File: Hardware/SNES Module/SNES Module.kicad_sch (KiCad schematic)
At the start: 4 parts, among them J1 Conn_01x31_Pin, J2 Conn_01x31_Pin, J3 Conn_02x31_Top_Bottom

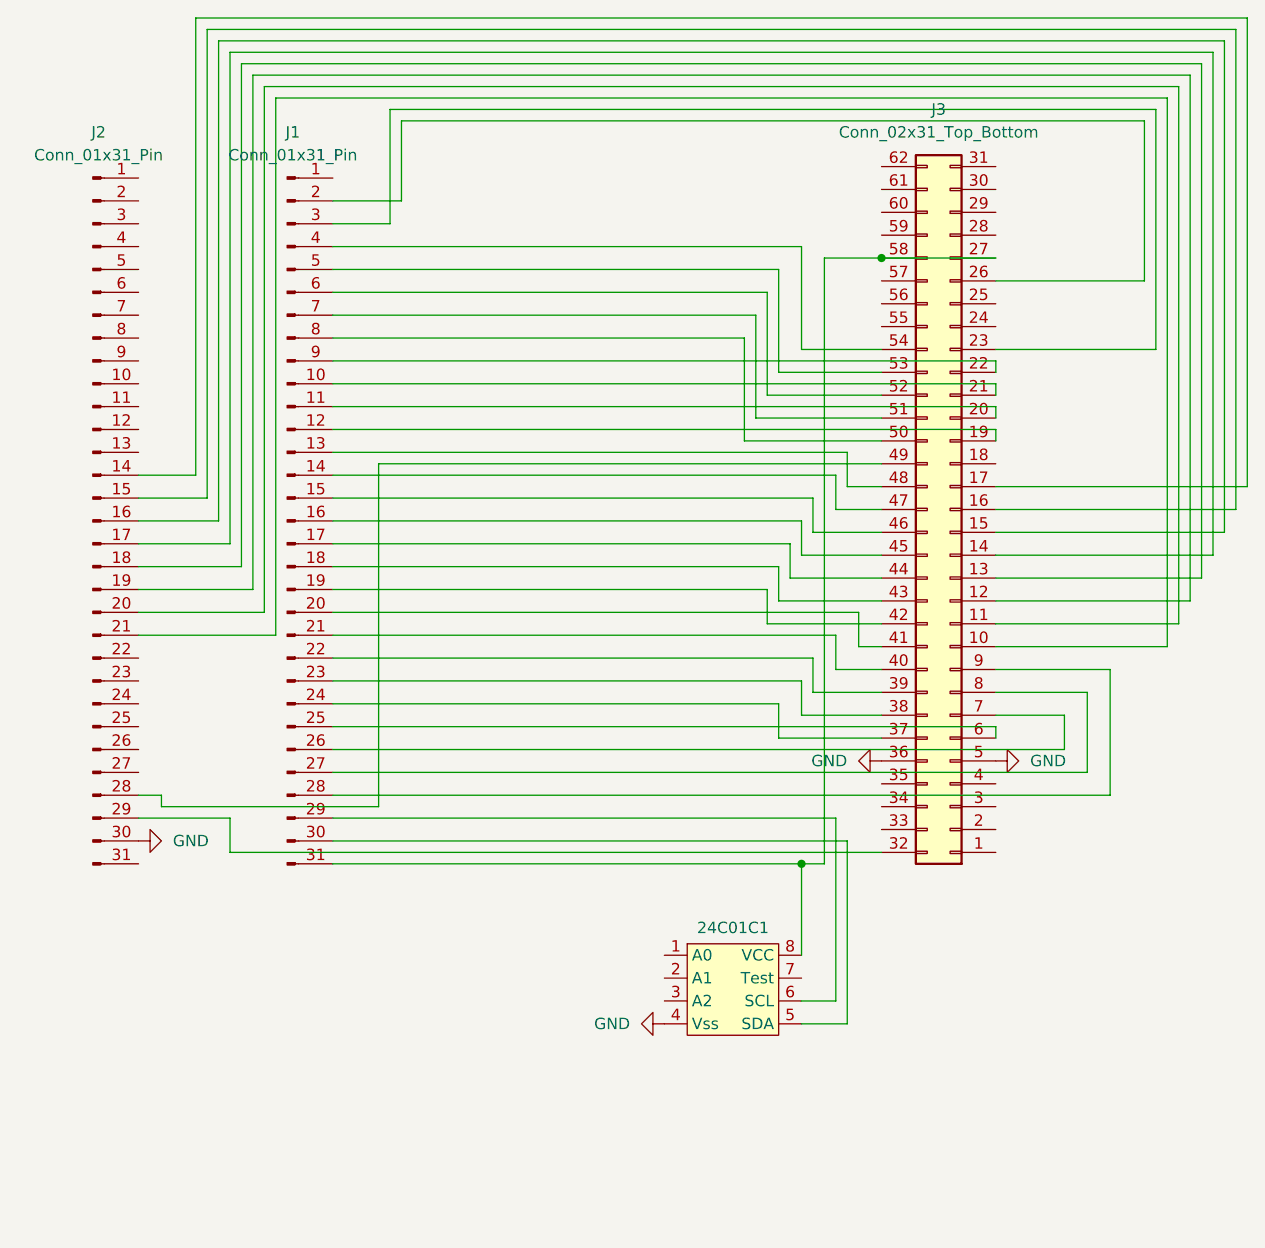
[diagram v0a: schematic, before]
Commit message: Setup Check Health menu, and remade the SNES Module PCB.
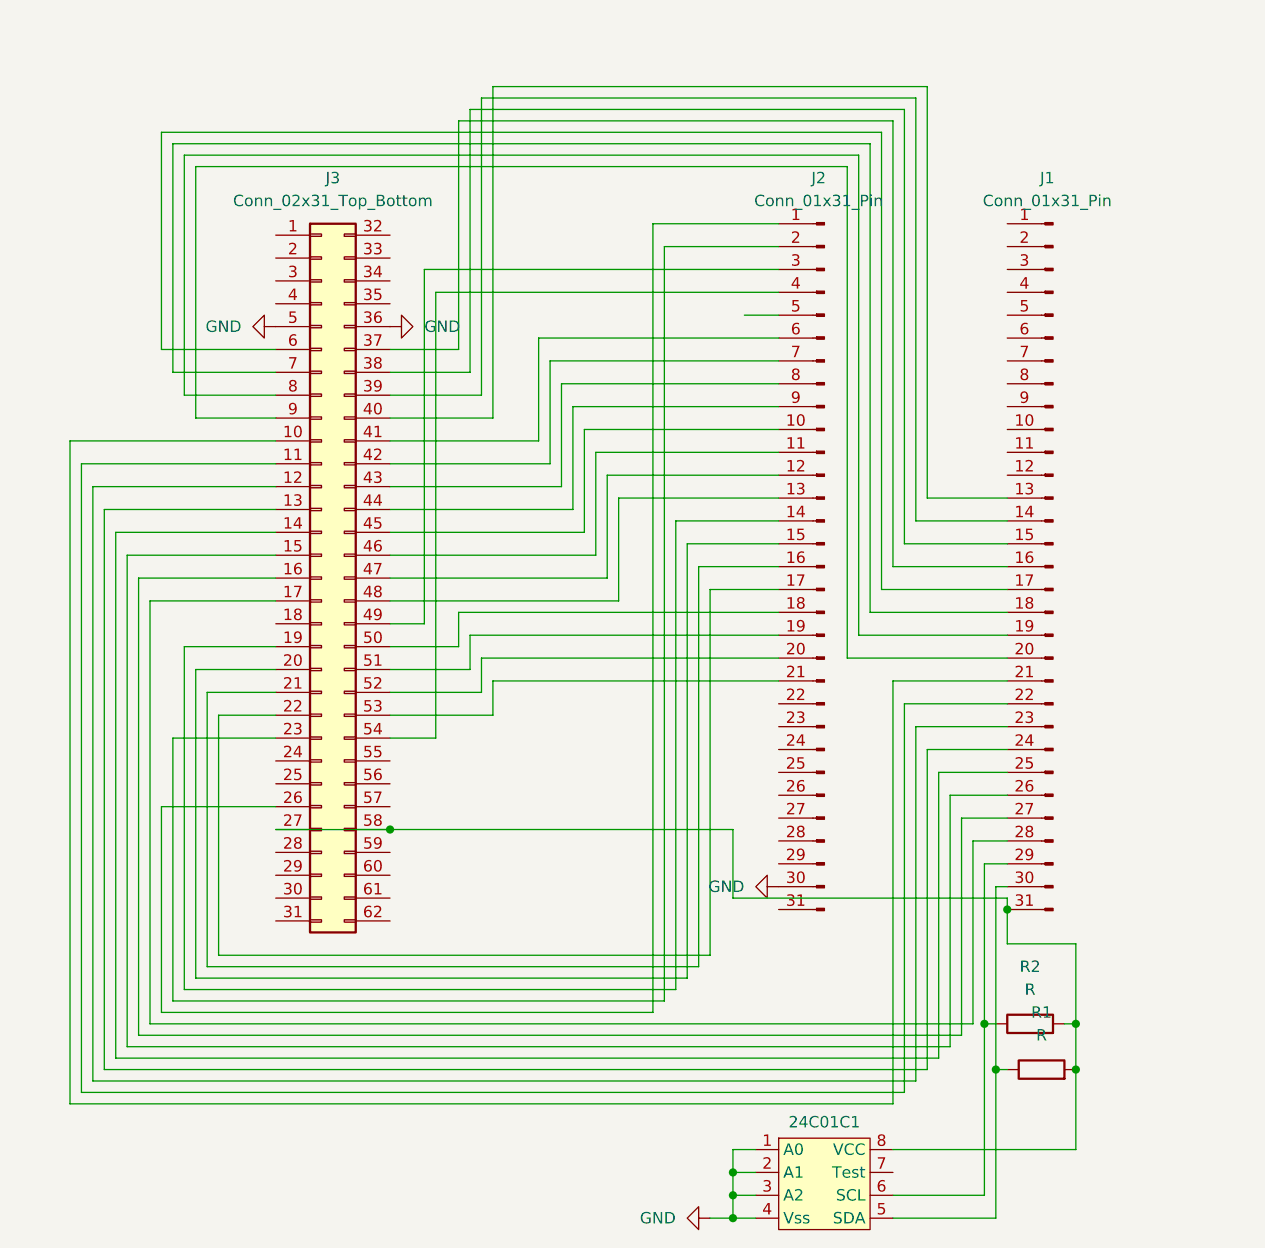
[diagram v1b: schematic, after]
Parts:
- added R1, R2: R, Resistor_THT:R_Axial_DIN0207_L6.3mm_D2.5mm_P10.16mm_Horizontal, symbol Device:R
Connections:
- net GND: now also 24C01C1.1 (A0), 24C01C1.2 (A1), 24C01C1.3 (A2)
- net at J1.10 (Pin_10): no longer J3.21 (Pin_21)
- net at J1.11 (Pin_11): no longer J3.20 (Pin_20)
- net at J1.12 (Pin_12): no longer J3.19 (Pin_19)
- net at J1.13 (Pin_13): now also J3.40 (Pin_40); no longer J3.48 (Pin_48)
- net at J1.14 (Pin_14): now also J3.39 (Pin_39); no longer J3.47 (Pin_47)
- net at J1.15 (Pin_15): now also J3.38 (Pin_38); no longer J3.46 (Pin_46)
- net at J1.16 (Pin_16): now also J3.37 (Pin_37); no longer J3.45 (Pin_45)
- net at J1.17 (Pin_17): now also J3.6 (Pin_6); no longer J3.44 (Pin_44)
- net at J1.18 (Pin_18): now also J3.7 (Pin_7); no longer J3.43 (Pin_43)
- net at J1.19 (Pin_19): now also J3.8 (Pin_8); no longer J3.42 (Pin_42)
- net at J1.2 (Pin_2): no longer J3.26 (Pin_26)
- net at J1.20 (Pin_20): now also J3.9 (Pin_9); no longer J3.41 (Pin_41)
- net at J1.21 (Pin_21): now also J3.10 (Pin_10); no longer J3.40 (Pin_40)
- net at J1.22 (Pin_22): now also J3.11 (Pin_11); no longer J3.39 (Pin_39)
- net at J1.23 (Pin_23): now also J3.12 (Pin_12); no longer J3.38 (Pin_38)
- net at J1.24 (Pin_24): now also J3.13 (Pin_13); no longer J3.37 (Pin_37)
- net at J1.25 (Pin_25): now also J3.14 (Pin_14); no longer J3.6 (Pin_6)
- net at J1.26 (Pin_26): now also J3.15 (Pin_15); no longer J3.7 (Pin_7)
- net at J1.27 (Pin_27): now also J3.16 (Pin_16); no longer J3.8 (Pin_8)
- net at J1.28 (Pin_28): now also J3.17 (Pin_17); no longer J3.9 (Pin_9)
- net at 24C01C1.6 (SCL), J1.29 (Pin_29): now also R2.1
- net at J1.3 (Pin_3): no longer J3.23 (Pin_23)
- net at 24C01C1.5 (SDA), J1.30 (Pin_30): now also R1.1
- net at 24C01C1.8 (VCC), J1.31 (Pin_31), J3.27 (Pin_27)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: now also R1.2, R2.2
- net at J1.4 (Pin_4): no longer J3.54 (Pin_54)
- net at J1.5 (Pin_5): no longer J3.53 (Pin_53)
- net at J1.6 (Pin_6): no longer J3.52 (Pin_52)
- net at J1.7 (Pin_7): no longer J3.51 (Pin_51)
- net at J1.8 (Pin_8): no longer J3.50 (Pin_50)
- net at J1.9 (Pin_9): no longer J3.22 (Pin_22)
- net at J2.1 (Pin_1): now also J3.26 (Pin_26)
- net at J2.10 (Pin_10): now also J3.45 (Pin_45)
- net at J2.11 (Pin_11): now also J3.46 (Pin_46)
- net at J2.12 (Pin_12): now also J3.47 (Pin_47)
- net at J2.13 (Pin_13): now also J3.48 (Pin_48)
- net at J2.14 (Pin_14): now also J3.19 (Pin_19); no longer J3.17 (Pin_17)
- net at J2.15 (Pin_15): now also J3.20 (Pin_20); no longer J3.16 (Pin_16)
- net at J2.16 (Pin_16): now also J3.21 (Pin_21); no longer J3.15 (Pin_15)
- net at J2.17 (Pin_17): now also J3.22 (Pin_22); no longer J3.14 (Pin_14)
- net at J2.18 (Pin_18): now also J3.50 (Pin_50); no longer J3.13 (Pin_13)
- net at J2.19 (Pin_19): now also J3.51 (Pin_51); no longer J3.12 (Pin_12)
- net at J2.2 (Pin_2): now also J3.23 (Pin_23)
- net at J2.20 (Pin_20): now also J3.52 (Pin_52); no longer J3.11 (Pin_11)
- net at J2.21 (Pin_21): now also J3.53 (Pin_53); no longer J3.10 (Pin_10)
- net at J2.28 (Pin_28): no longer J3.49 (Pin_49)
- net at J2.29 (Pin_29): no longer J3.32 (Pin_32)
- net at J2.3 (Pin_3): now also J3.49 (Pin_49)
- net at J2.4 (Pin_4): now also J3.54 (Pin_54)
- net at J2.6 (Pin_6): now also J3.41 (Pin_41)
- net at J2.7 (Pin_7): now also J3.42 (Pin_42)
- net at J2.8 (Pin_8): now also J3.43 (Pin_43)
- net at J2.9 (Pin_9): now also J3.44 (Pin_44)
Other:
- moved on the sheet: 24C01C1, J1, J2, J3
